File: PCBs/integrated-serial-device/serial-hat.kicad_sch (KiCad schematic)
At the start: 22 parts, among them CN1 Modem port, CN2 Modem out 3, CN3 Printer port, J1 Rpi headers, J3 Conn_01x02_Pin, K1 Quicktake, K2 ImageWriter, SW1 Modem To Proxy, SW2 Modem to Quicktake, SW3 Modem out 3, SW4 Printer out 3, SW5 Printer to Proxy, SW6 Printer to ImageWriter, SW7 SW_SPST, SW8 SW_Slide_DPDT, U1 MAX3232

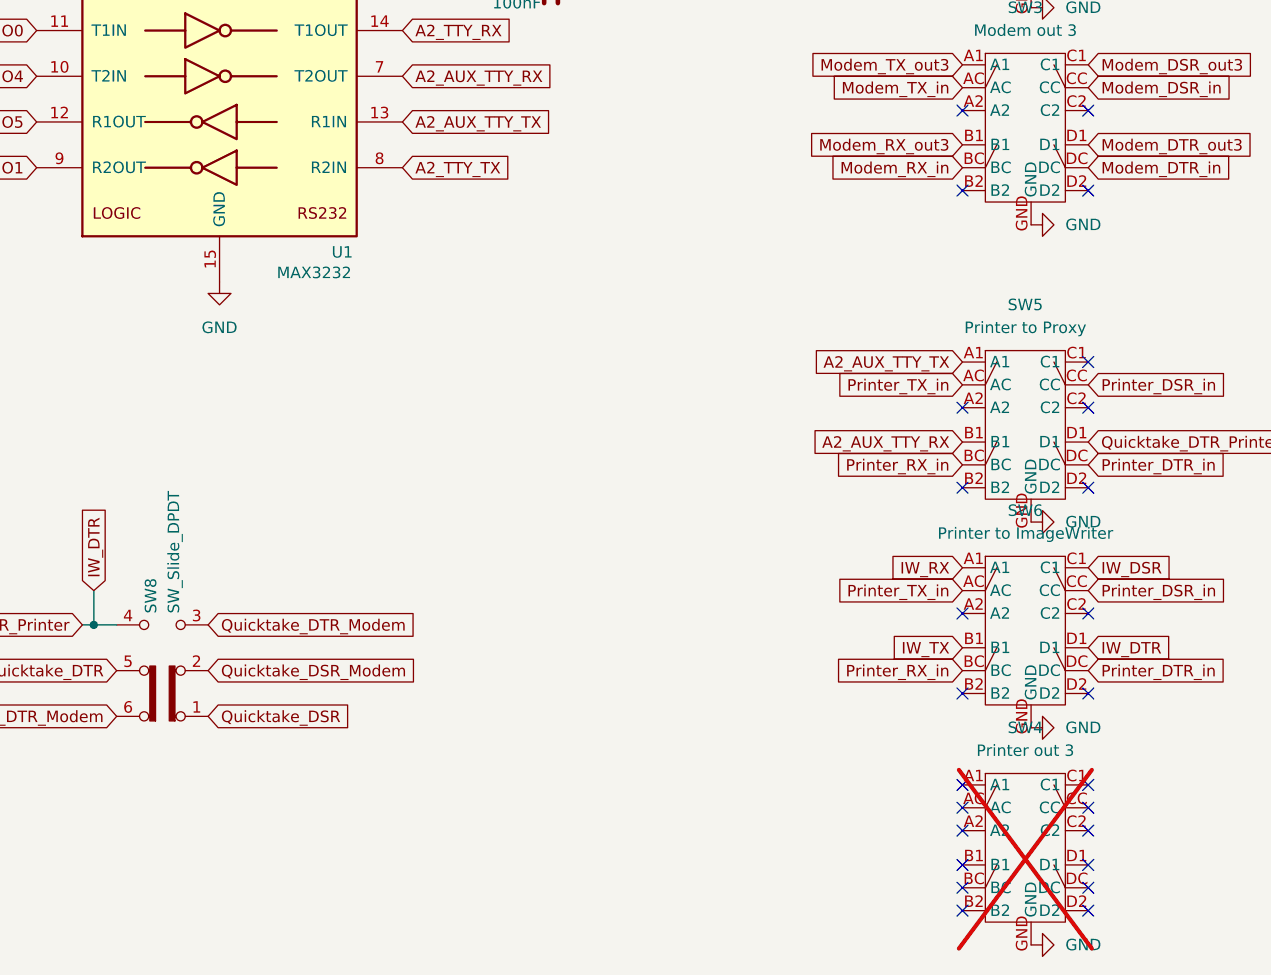
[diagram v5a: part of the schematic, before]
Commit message: Add references
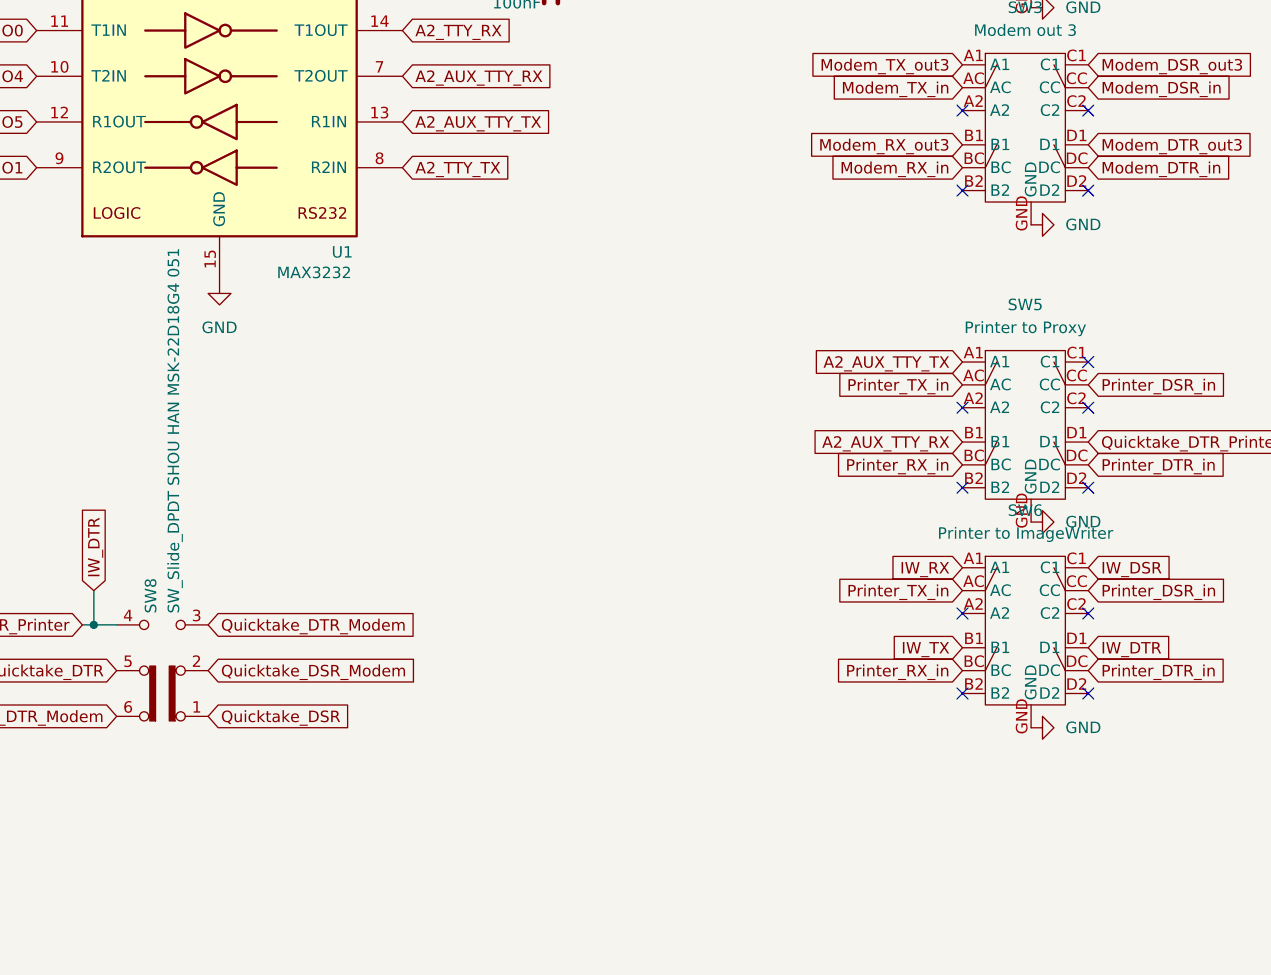
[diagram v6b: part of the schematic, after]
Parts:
- removed SW4: Printer out 3, DIN5:4PDT piano switch, symbol DIN:4PDT_switch
- SW7: LCSC (none) -> C6575016
- SW8: value SW_Slide_DPDT -> SW_Slide_DPDT SHOU HAN MSK-22D18G4 051; LCSC (none) -> C7507433
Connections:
- no-connect marks 57 -> 45
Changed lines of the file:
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@@
 	)
 	(no_connect
-		(at 261.62 160.02)
-	)
-	(no_connect
-		(at 247.65 153.67)
-	)
-	(no_connect
 		(at 100.33 86.36)
 	)
 	(no_connect
-		(at 247.65 157.48)
-	)
-	(no_connect
 		(at 100.33 50.8)
 	)
 	(no_connect
-		(at 261.62 151.13)
-	)
-	(no_connect
 		(at 247.65 129.54)
 	)
@@
 	)
 	(no_connect
-		(at 247.65 148.59)
-	)
-	(no_connect
-		(at 261.62 162.56)
-	)
-	(no_connect
 		(at 33.02 77.47)
 	)
@@
 	)
 	(no_connect
-		(at 247.65 160.02)
-	)
-	(no_connect
 		(at 247.65 26.67)
 	)
 	(no_connect
-		(at 247.65 162.56)
-	)
-	(no_connect
 		(at 247.65 58.42)
 	)
@@
 	)
 	(no_connect
-		(at 247.65 151.13)
-	)
-	(no_connect
-		(at 261.62 157.48)
-	)
-	(no_connect
 		(at 87.63 78.74)
 	)
@@
 	)
 	(no_connect
-		(at 261.62 148.59)
-	)
-	(no_connect
 		(at 100.33 66.04)
 	)
@@
 	)
 	(no_connect
-		(at 261.62 153.67)
-	)
-	(no_connect
 		(at 100.33 81.28)
 	)
@@
 			)
 		)
+		(property "LCSC" "C6575016"
+			(at 92.71 118.11 0)
+			(effects
+				(font
+					(size 1.27 1.27)
+				)
+				(hide yes)
+			)
+		)
 		(pin "2"
 		)
@@
 			)
 		)
-		(property "Value" "SW_Slide_DPDT"
+		(property "Value" "SW_Slide_DPDT SHOU HAN MSK-22D18G4 051"
 			(at 160.0199 129.54 90)
 			(effects
@@
 			)
 		)
+		(property "LCSC" "C7507433"
+			(at 158.75 135.89 90)
+			(effects
+				(font
+					(size 1.27 1.27)
+				)
+				(hide yes)
+			)
+		)
 		(pin "1"
 		)
@@
 			)
 		)
-		(property "Description" ""
+		(property "Description" "https://www.alibaba.com/product-detail/Interlocking-Key-Push-Button-Switches-6_1601722717319.html"
 			(at 251.46 66.04 0)
 			(effects
@@
 			)
 		)
-		(property "Description" ""
+		(property "Description" "https://www.alibaba.com/product-detail/Interlocking-Key-Push-Button-Switches-6_1601722717319.html"
 			(at 251.46 19.05 0)
 			(effects
@@
 			)
 		)
-		(property "Description" ""
+		(property "Description" "https://www.alibaba.com/product-detail/Interlocking-Key-Push-Button-Switches-6_1601722717319.html"
 			(at 251.46 99.06 0)
 			(effects
@@
 			)
 		)
-		(property "Description" ""
+		(property "Description" "https://www.alibaba.com/product-detail/Interlocking-Key-Push-Button-Switches-6_1601722717319.html"
 			(at 251.46 121.92 0)
 			(effects
@@
 			)
 		)
-		(property "Description" ""
+		(property "Description" "https://www.alibaba.com/product-detail/Interlocking-Key-Push-Button-Switches-6_1601722717319.html"
 			(at 251.46 41.91 0)
 			(effects
@@
 	(symbol
 		(lib_id "power:GND")
-		(at 255.27 166.37 90)
-		(unit 1)
-		(exclude_from_sim no)
-		(in_bom yes)
-		(on_board yes)
-		(dnp no)
-		(fields_autoplaced yes)
-		(property "Reference" "#PWR027"
-			(at 261.62 166.37 0)
-			(effects
-				(font
-					(size 1.27 1.27)
-				)
-				(hide yes)
-			)
-		)
-		(property "Value" "GND"
-			(at 259.08 166.3699 90)
-			(effects
-				(font
-					(size 1.27 1.27)
-				)
-				(justify right)
-			)
-		)
-		(property "Footprint" ""
-			(at 255.27 166.37 0)
-			(effects
-				(font
-					(size 1.27 1.27)
-				)
-				(hide yes)
-			)
-		)
-		(property "Datasheet" ""
-			(at 255.27 166.37 0)
-			(effects
-				(font
-					(size 1.27 1.27)
-				)
-				(hide yes)
-			)
-		)
-		(property "Description" "Power symbol creates a global label with name \"GND\" , ground"
-			(at 255.27 166.37 0)
-			(effects
-				(font
-					(size 1.27 1.27)
-				)
-				(hide yes)
-			)
-		)
-		(pin "1"
-		)
-		(instances
-			(project "serial-hat"
-				(path "/f30a5902-bf77-48c6-ab50-b8e2235ec207"
-					(reference "#PWR027")
-					(unit 1)
-				)
-			)
-		)
-	)
-	(symbol
-		(lib_id "power:GND")
 		(at 90.17 101.6 270)
 		(unit 1)
@@
 					(unit 1)
 				)
-			)
-		)
-	)
-	(symbol
-		(lib_id "DIN:4PDT_switch")
-		(at 251.46 146.05 0)
-		(unit 1)
-		(exclude_from_sim no)
-		(in_bom yes)
-		(on_board yes)
-		(dnp yes)
-		(fields_autoplaced yes)
-		(property "Reference" "SW4"
-			(at 254.635 142.24 0)
-			(effects
-				(font
-					(size 1.27 1.27)
-				)
-			)
-		)
-		(property "Value" "Printer out 3"
-			(at 254.635 144.78 0)
-			(effects
-				(font
-					(size 1.27 1.27)
-				)
-			)
-		)
-		(property "Footprint" "DIN5:4PDT piano switch"
-			(at 251.46 146.05 0)
-			(effects
-				(font
-					(size 1.27 1.27)
-				)
-				(hide yes)
-			)
-		)
-		(property "Datasheet" ""
-			(at 251.46 146.05 0)
-			(effects
-				(font
-					(size 1.27 1.27)
-				)
-				(hide yes)
-			)
-		)
-		(property "Description" ""
-			(at 251.46 146.05 0)
-			(effects
-				(font
-					(size 1.27 1.27)
-				)
-				(hide yes)
-			)
-		)
-		(pin "D1"
-		)
-		(pin "C2"
-		)
-		(pin "B1"
-		)
-		(pin "CC"
-		)
-		(pin "AC"
-		)
-		(pin "A1"
-		)
-		(pin "BC"
-		)
-		(pin "B2"
-		)
-		(pin "C1"
-		)
-		(pin "D2"
-		)
-		(pin "A2"
-		)
-		(pin "DC"
-		)
-		(pin "GND"
-		)
-		(instances
-			(project "serial-hat"
-				(path "/f30a5902-bf77-48c6-ab50-b8e2235ec207"
-					(reference "SW4")
-					(unit 1)
-				)

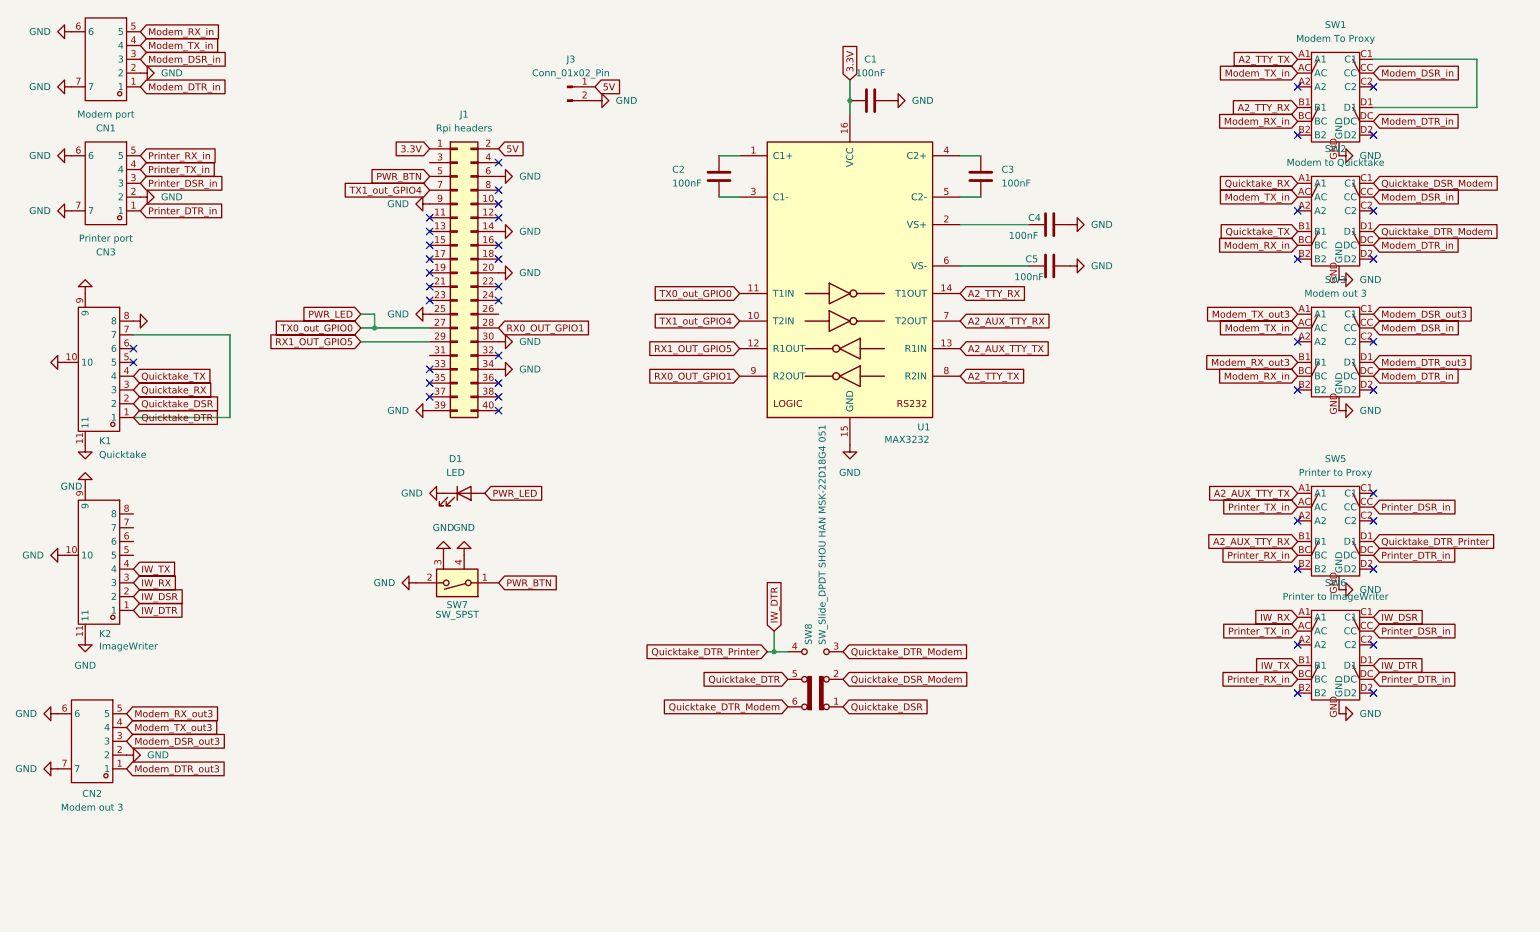
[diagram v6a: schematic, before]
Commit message: Add gpio-fan ability
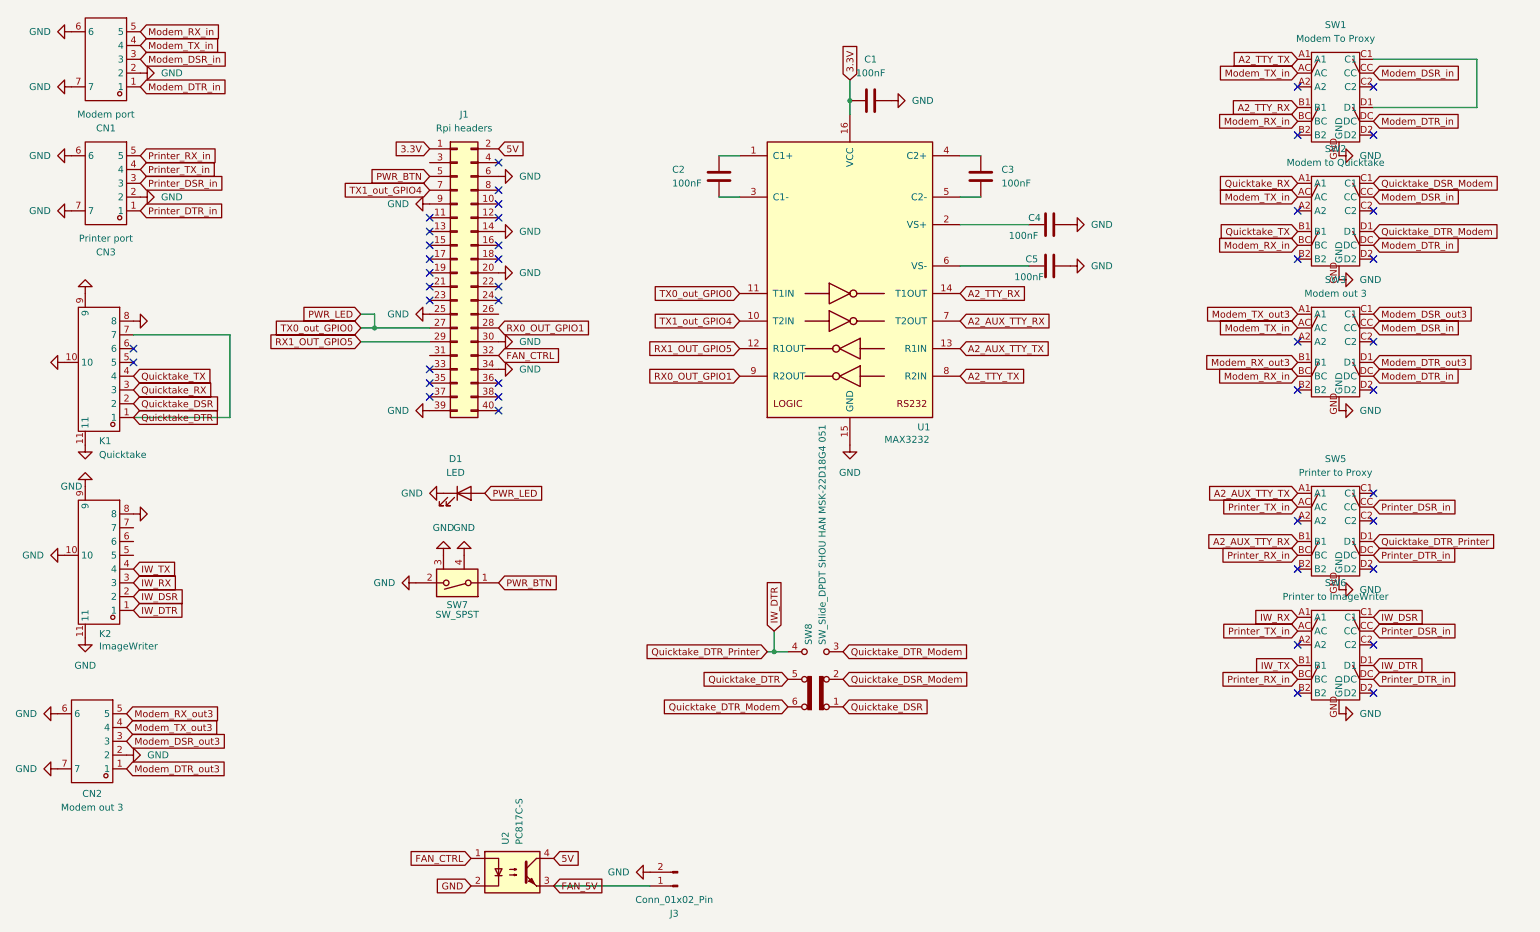
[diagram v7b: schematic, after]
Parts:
- added U2: PC817C-S, Package_SO:SOP-4_3.8x4.1mm_P2.54mm, symbol Isolator:PC817
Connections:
- net 5V: now also U2.4; no longer J3.1 (Pin_1)
- net GND: now also K2.8, U2.2
- net FAN_CTRL: now reaches J1.32 (Pin_32)
- net FAN_CTRL: now also U2.1
- new net FAN_5V: J3.1 (Pin_1), U2.3
- no-connect marks 45 -> 44
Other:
- moved on the sheet: J3

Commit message: Update to new lib
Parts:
- CN1, CN2, CN3: footprint DIN5:CONN-TH_DIN-504-M10 -> Colins-Kicad:DIN-5-M C23689428; symbol DIN:DIN-504 -> Colins-Kicad:DIN-5_180degree
- K1, K2: footprint DIN5:MINI-DIN8 -> Colins-Kicad:MINI-DIN8-F C20611694; symbol DIN:DIN-802 -> Colins-Kicad:Serial_Mini-DIN-8
- SW1, SW2, SW3, SW5, SW6: footprint DIN5:4PDT piano switch -> Colins-Kicad:4PDT 12 pins Piano Switch; symbol DIN:4PDT_switch -> Colins-Kicad:4PDT_switch
- SW7: footprint DIN5:SPST_power_switch -> Colins-Kicad:SPST momentary switch C6575016
- SW8: footprint DIN5:DPDT slide switch C7507433 -> Colins-Kicad:DPDT slide switch C7507433
- U2: footprint Package_SO:SOP-4_3.8x4.1mm_P2.54mm -> Colins-Kicad:PC817C-S C3008369
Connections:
- no-connect marks 44 -> 47
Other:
- moved on the sheet: J1, J3, SW7, U2
